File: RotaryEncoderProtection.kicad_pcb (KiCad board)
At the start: 2 copper layers, 39 x 32 mm, 14 parts, among them J1 DE9_Plug_MountingHoles, J2 Conn_01x01, J3 Conn_01x04

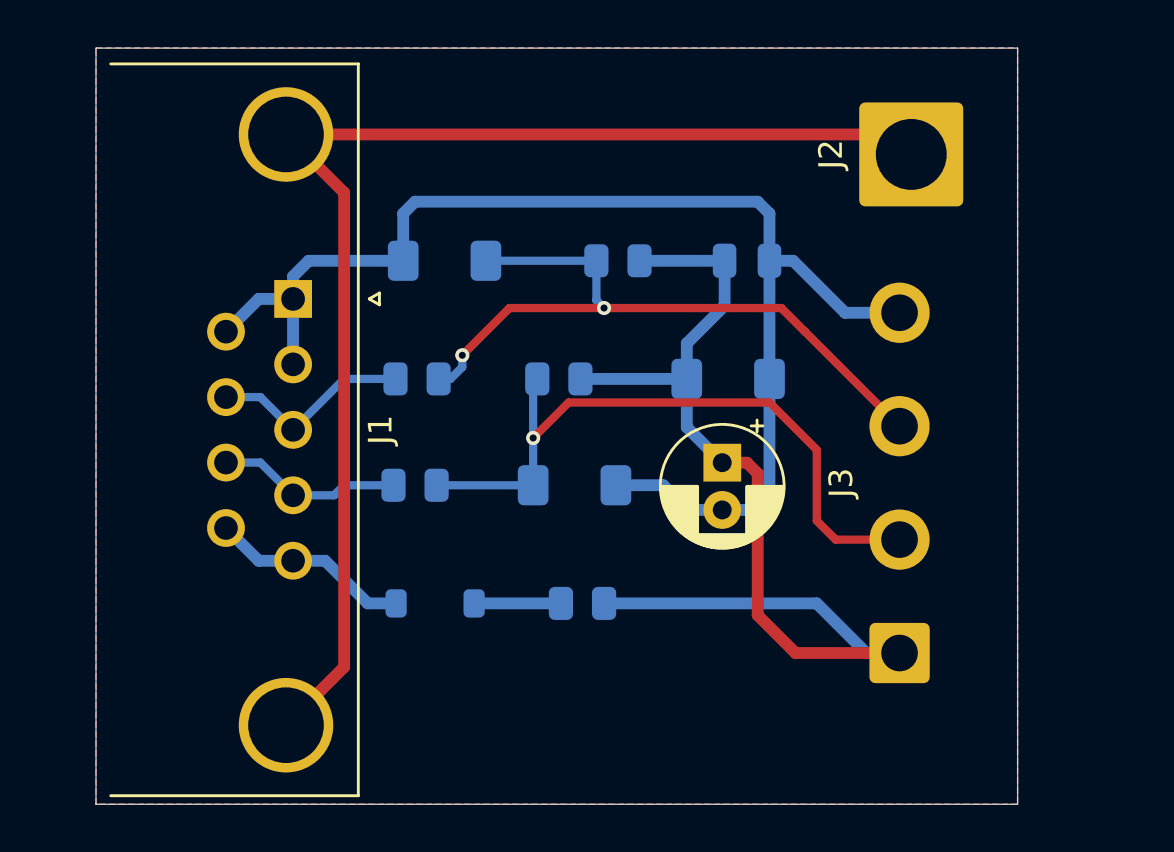
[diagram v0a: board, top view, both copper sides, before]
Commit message: removed traces, where zones are; added text, logos, copyright; added Reichelt article numbvers
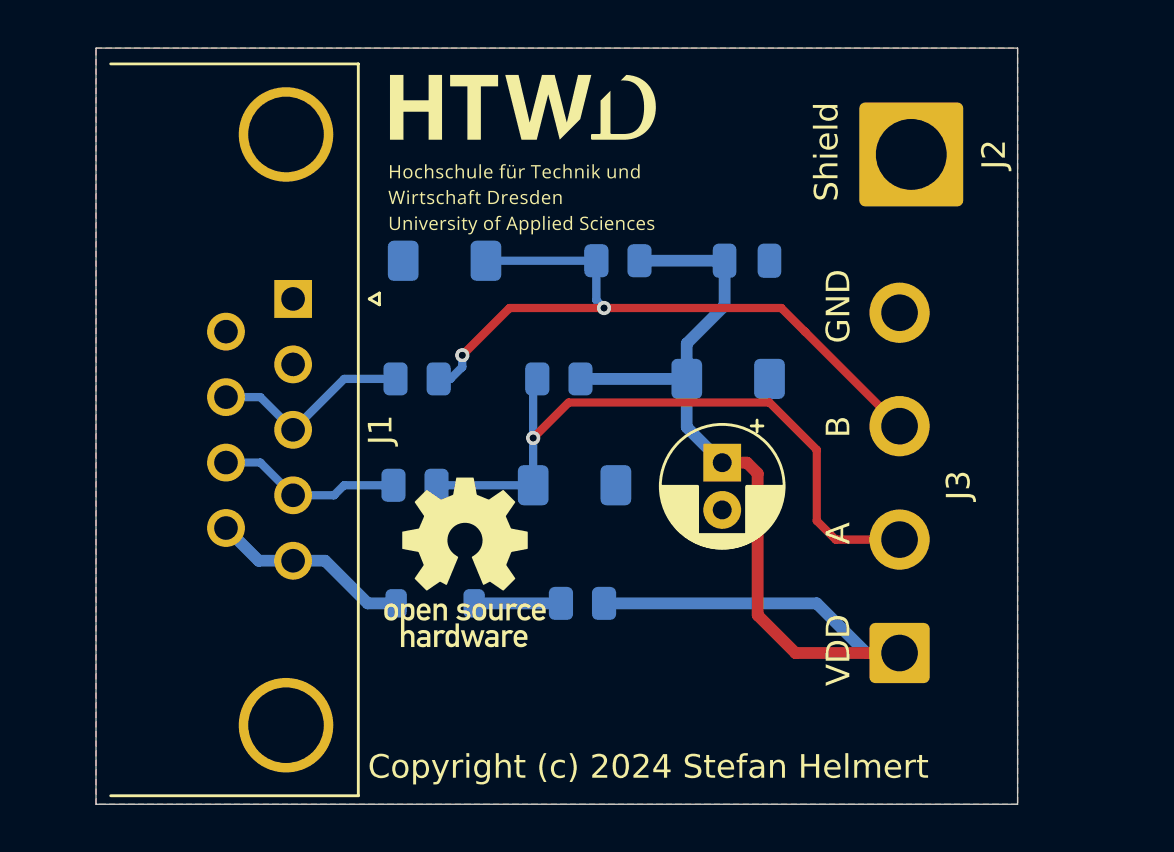
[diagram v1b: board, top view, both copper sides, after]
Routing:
- net GND: track 55.6 -> 0.00 mm
- net /Shield: track 53.8 -> 0.00 mm
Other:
- board text added: "A"
- board text added: "B"
- board text added: "Copyright (c) 2024 Stefan Helmert"
- board text added: "GND"
- board text added: "Shield"
- board text added: "VDD"

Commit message: optimized silkscreen
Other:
- board text added: "Black"
- board text added: "Green"
- board text added: "Red"
- board text added: "Silver"
- board text added: "White"
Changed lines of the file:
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@@
 		(tags "connector wire 2.5sqmm")
 		(property "Reference" "J2"
-			(at 0 3.5 90)
+			(at 3.5 0 180)
 			(layer "F.SilkS")
 			(effects
@@
 		(tags "CP Radial series Radial pin pitch 2.00mm  diameter 5mm Electrolytic Capacitor")
 		(property "Reference" "C2"
-			(at 1 -3.75 90)
+			(at 0.955112 3.5 90)
 			(layer "F.SilkS")
-			(hide yes)
 			(effects
 				(font
@@
 		)
 		(property "Value" "22u"
-			(at 1 3.75 90)
+			(at 1 -3.5 90)
 			(layer "F.Fab")
 			(effects
@@
 		)
 		(fp_text user "${REFERENCE}"
-			(at 1 0 90)
+			(at 0.955112 0 90)
 			(layer "F.Fab")
 			(effects
@@
 		(tags "connector wire 0.75sqmm")
 		(property "Reference" "J3"
-			(at 7.1 2.495 90)
+			(at 7.1 -1.505 90)
 			(layer "F.SilkS")
 			(effects
@@
 		(tags "resistor")
 		(property "Reference" "R2"
-			(at 0 1.65 0)
+			(at 0 -1.5 0)
 			(layer "B.SilkS")
 			(effects
@@
 		(tags "Diode Mini-MELF (SOD-80)")
 		(property "Reference" "D4"
-			(at 0 2 0)
+			(at 0 -2 0)
 			(layer "B.SilkS")
 			(effects
@@
 		(tags "resistor")
 		(property "Reference" "R1"
-			(at 0 1.65 0)
+			(at 0 -1.5 0)
 			(layer "B.SilkS")
 			(effects
@@
 		(tags "resistor")
 		(property "Reference" "R3"
-			(at 0 1.65 0)
+			(at 0 -1.5 0)
 			(layer "B.SilkS")
 			(effects
@@
 		(tags "capacitor")
 		(property "Reference" "C1"
-			(at 0 1.68 0)
+			(at 0 -1.5 0)
 			(layer "B.SilkS")
 			(effects
@@
 		(tags "Diode Mini-MELF (SOD-80)")
 		(property "Reference" "D2"
-			(at 0 2 0)
+			(at 0 -2 0)
 			(layer "B.SilkS")
 			(effects
@@
 		)
 	)
+	(gr_text "Black"
+		(at 103 52 90)
+		(layer "B.SilkS")
+		(effects
+			(font
+				(size 1 1)
+				(thickness 0.1)
+			)
+			(justify left bottom mirror)
+		)
+	)
+	(gr_text "White"
+		(at 103 57 90)
+		(layer "B.SilkS")
+		(effects
+			(font
+				(size 1 1)
+				(thickness 0.1)
+			)
+			(justify left bottom mirror)
+		)
+	)
+	(gr_text "Red"
+		(at 103 67 90)
+		(layer "B.SilkS")
+		(effects
+			(font
+				(size 1 1)
+				(thickness 0.1)
+			)
+			(justify left bottom mirror)
+		)
+	)
+	(gr_text "Green"
+		(at 103 61.5 90)
+		(layer "B.SilkS")
+		(effects
+			(font
+				(size 1 1)
+				(thickness 0.1)
+			)
+			(justify left bottom mirror)
+		)
+	)
 	(gr_text "Shield"
 		(at 97.5 45 90)
@@
 		)
 	)
+	(gr_text "Silver"
+		(at 104.5 45.5 90)
+		(layer "B.SilkS")
+		(effects
+			(font
+				(size 1 1)
+				(thickness 0.1)
+			)
+			(justify left bottom mirror)
+		)
+	)
 	(gr_text "VDD"
 		(at 98 67 90)
@@
 		)
 	)
+	(gr_text "Black"
+		(at 103 56 90)
+		(layer "F.SilkS")
+		(effects
+			(font
+				(size 1 1)
+				(thickness 0.1)
+			)
+			(justify left bottom)
+		)
+	)
 	(gr_text "Shield"
 		(at 97.5 49.5 90)
@@
 		)
 	)
+	(gr_text "Green"
+		(at 103 66 90)
+		(layer "F.SilkS")
+		(effects
+			(font
+				(size 1 1)
+				(thickness 0.1)
+			)
+			(justify left bottom)
+		)
+	)
+	(gr_text "White"
+		(at 103 61 90)
+		(layer "F.SilkS")
+		(effects
+			(font
+				(size 1 1)
+				(thickness 0.1)
+			)
+			(justify left bottom)
+		)
+	)
 	(gr_text "A"
 		(at 98 64 90)
@@
 		)
 	)
+	(gr_text "Silver"
+		(at 104.5 49.5 90)
+		(layer "F.SilkS")
+		(effects
+			(font
+				(size 1 1)
+				(thickness 0.1)
+			)
+			(justify left bottom)
+		)
+	)
 	(gr_text "Copyright (c) 2024 Stefan Helmert"
 		(at 77.5 74 0)
 		(layer "F.SilkS")
 		(effects
+			(font
+				(size 1 1)
+				(thickness 0.1)
+			)
+			(justify left bottom)
+		)
+	)
+	(gr_text "Red"
+		(at 103 70 90)
+		(layer "F.SilkS")
+		(effects

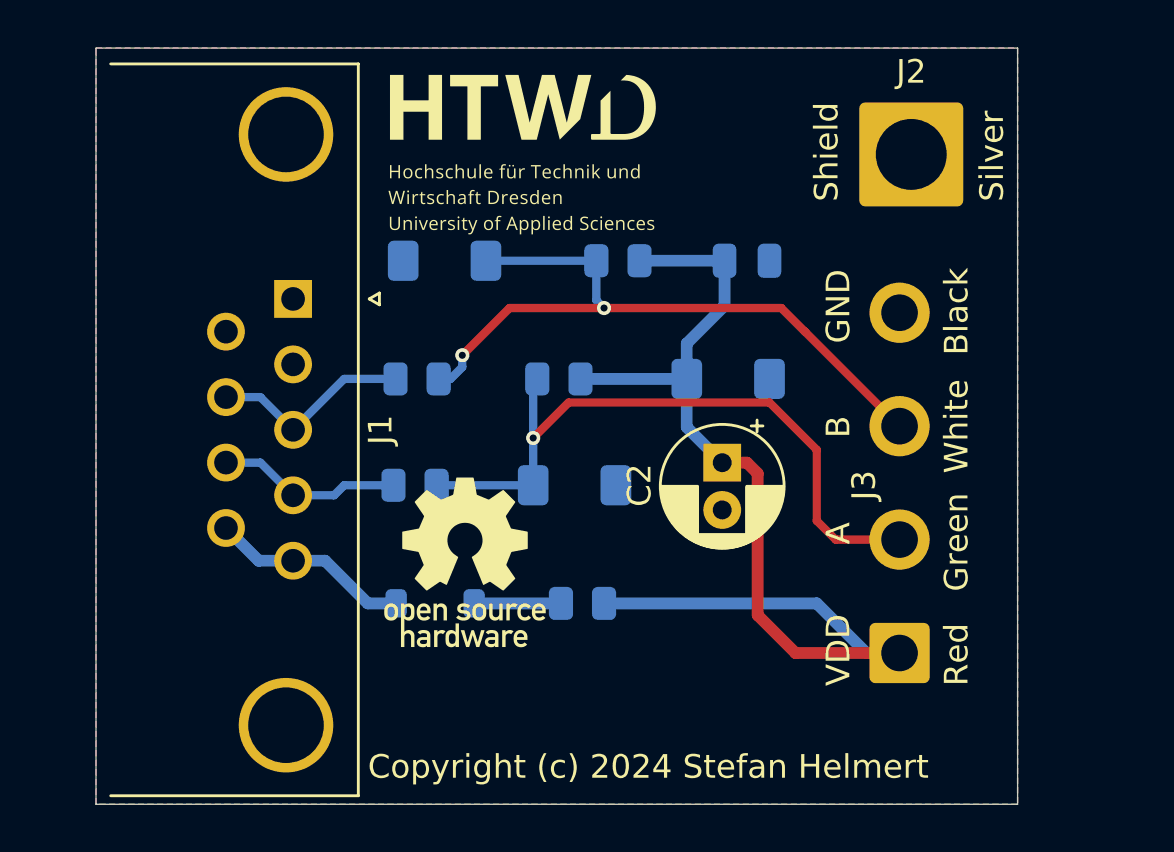
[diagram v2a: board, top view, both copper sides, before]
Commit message: smaller board
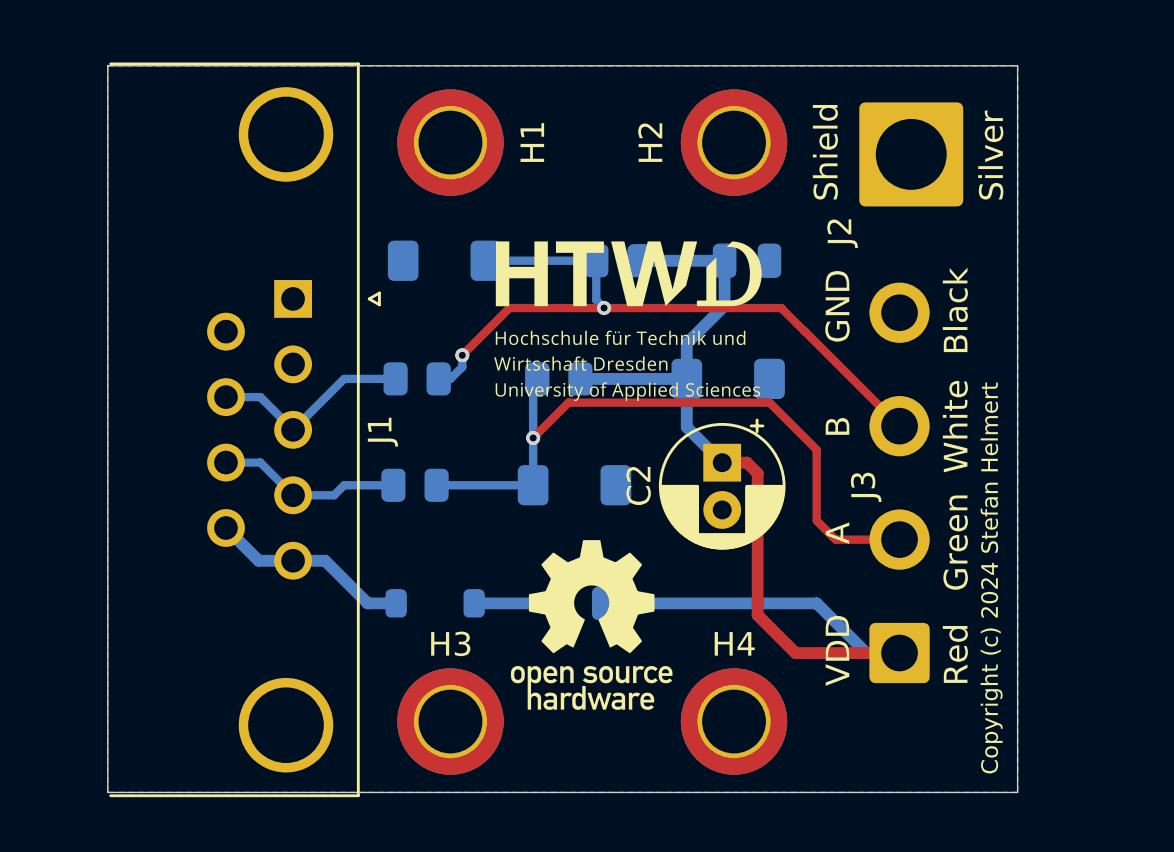
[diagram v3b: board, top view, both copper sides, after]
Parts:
- added H1: MountingHole_Pad, MountingHole:MountingHole_2.7mm_M2.5_ISO14580_Pad_TopBottom, F.Cu at (81.0, 47.0)
- added H2: MountingHole_Pad, MountingHole:MountingHole_2.7mm_M2.5_ISO14580_Pad_TopBottom, F.Cu at (93.0, 47.0)
- added H3: MountingHole_Pad, MountingHole:MountingHole_2.7mm_M2.5_ISO14580_Pad_TopBottom, F.Cu at (81.0, 71.5)
- added H4: MountingHole_Pad, MountingHole:MountingHole_2.7mm_M2.5_ISO14580_Pad_TopBottom, F.Cu at (93.0, 71.5)
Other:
- board size 39 x 32 mm -> 38.5 x 30.8 mm

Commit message: Digikey M3 D-Sub-9 Connector
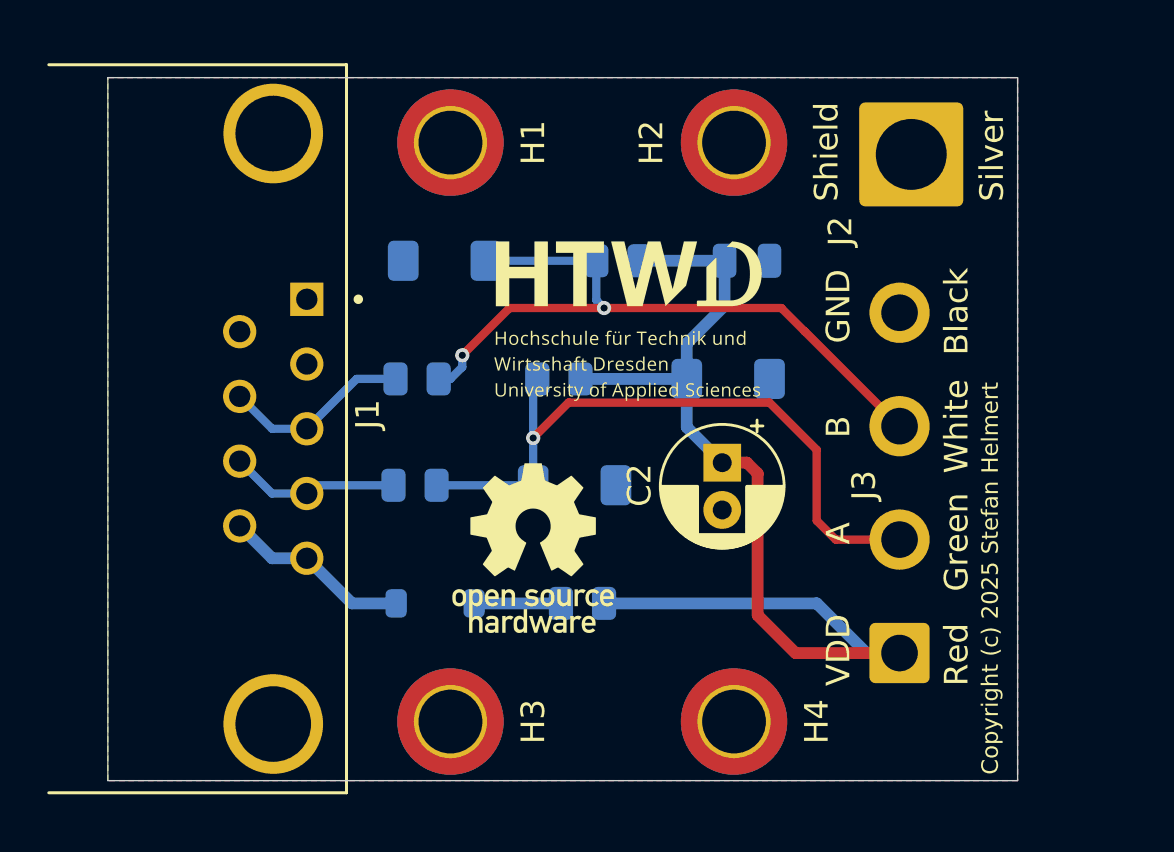
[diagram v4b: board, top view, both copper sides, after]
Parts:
- J1: footprint Connector_Dsub:DSUB-9_Male_Horizontal_P2.77x2.84mm_EdgePinOffset4.94mm_Housed_MountingHolesOffset7.48mm -> D09P33E4GL00LF_b:AMPHENOL_D09P33E4GL00LF
- moved J1 5.56 mm to (73.5, 59.1)
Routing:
- net /A: track 7.84 -> 7.22 mm
- net /B: track 8.64 -> 8.04 mm
- net VDC: track 8.52 -> 7.98 mm
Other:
- board size 38.5 x 30.8 mm -> 38.5 x 29.8 mm
- board text added: "Copyright (c) 2025 Stefan Helmert"
- board text removed: "Copyright (c) 2024 Stefan Helmert"

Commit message: new KiCad Standard D-Sub-9 Connector
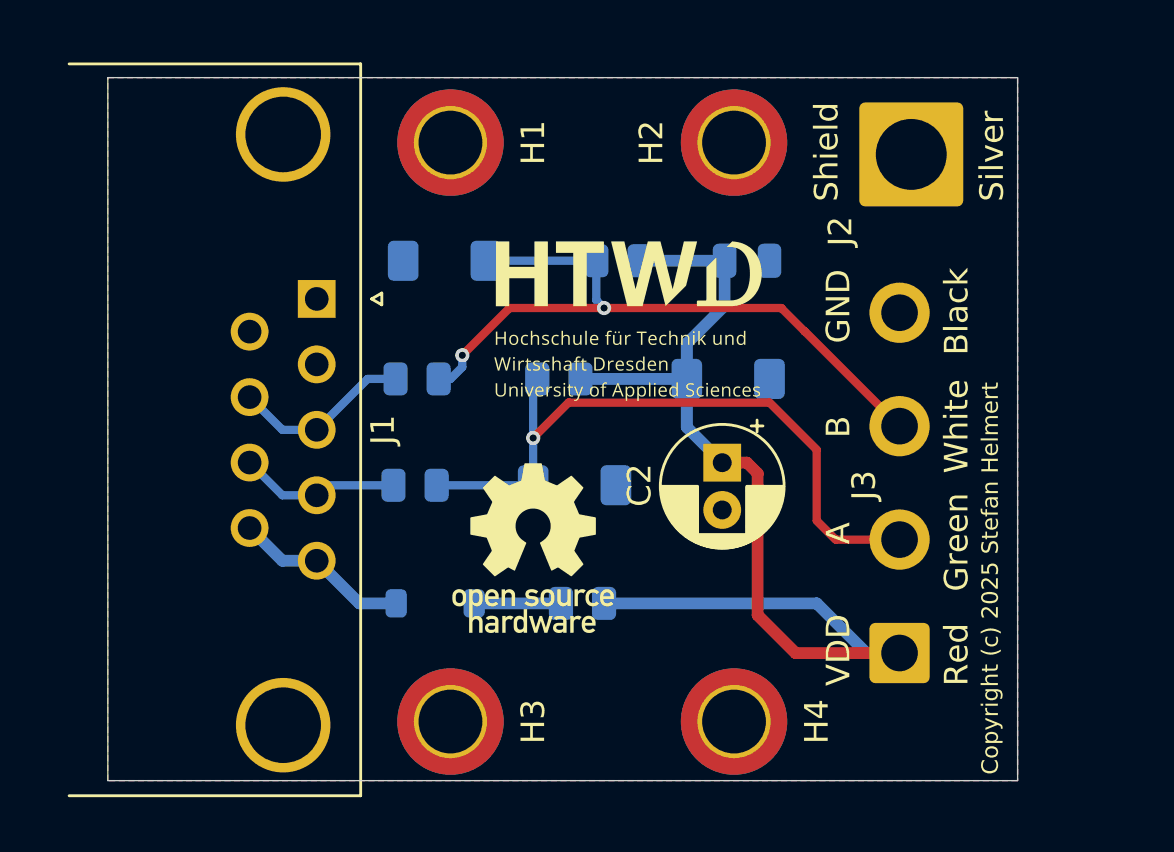
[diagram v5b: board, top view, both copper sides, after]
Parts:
- J1: footprint D09P33E4GL00LF_b:AMPHENOL_D09P33E4GL00LF -> Connector_Dsub:DSUB-9_Pins_Horizontal_P2.77x2.84mm_EdgePinOffset7.70mm_Housed_MountingHolesOffset9.12mm
- moved J1 5.79 mm to (75.3, 53.6)
